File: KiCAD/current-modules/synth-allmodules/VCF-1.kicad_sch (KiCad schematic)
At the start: 0 parts

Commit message: VCF-1 Components Placed
Additions:
- Basic components for VCF-1
Changes:
- None
Removals:
- None
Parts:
- added C50: C, symbol Device:C
- added C51: C_Polarized, symbol Device:C_Polarized
- added Q12: 2N3906, Package_TO_SOT_THT:TO-92_Inline, symbol Transistor_BJT:2N3906
- added R98: R, symbol Device:R
- added RV37: R_Potentiometer, symbol Device:R_Potentiometer
- added SW17: SW_SPST, symbol Switch:SW_SPST
- added U15: TL074, symbol Amplifier_Operational:TL074
- added U16, U17: CA3080, symbol Amplifier_Operational:CA3080
- added U18: TL072, symbol Amplifier_Operational:TL072

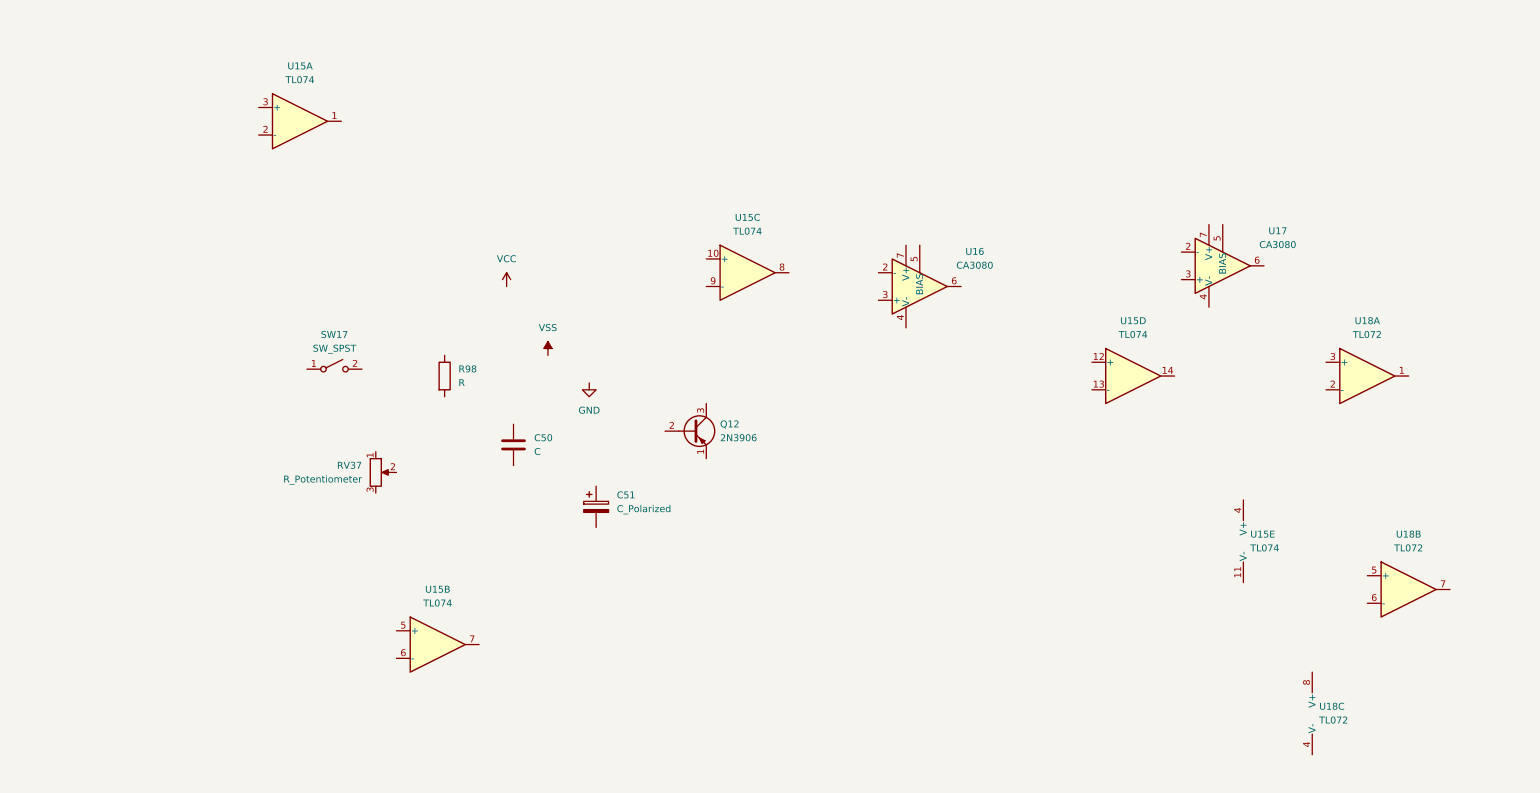
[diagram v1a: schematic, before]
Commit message: VCF-1 Component Placement
Additions:
- Most of the components for VCF-1 have been placed in the correct spots
Changes:
- None
Removals:
- None
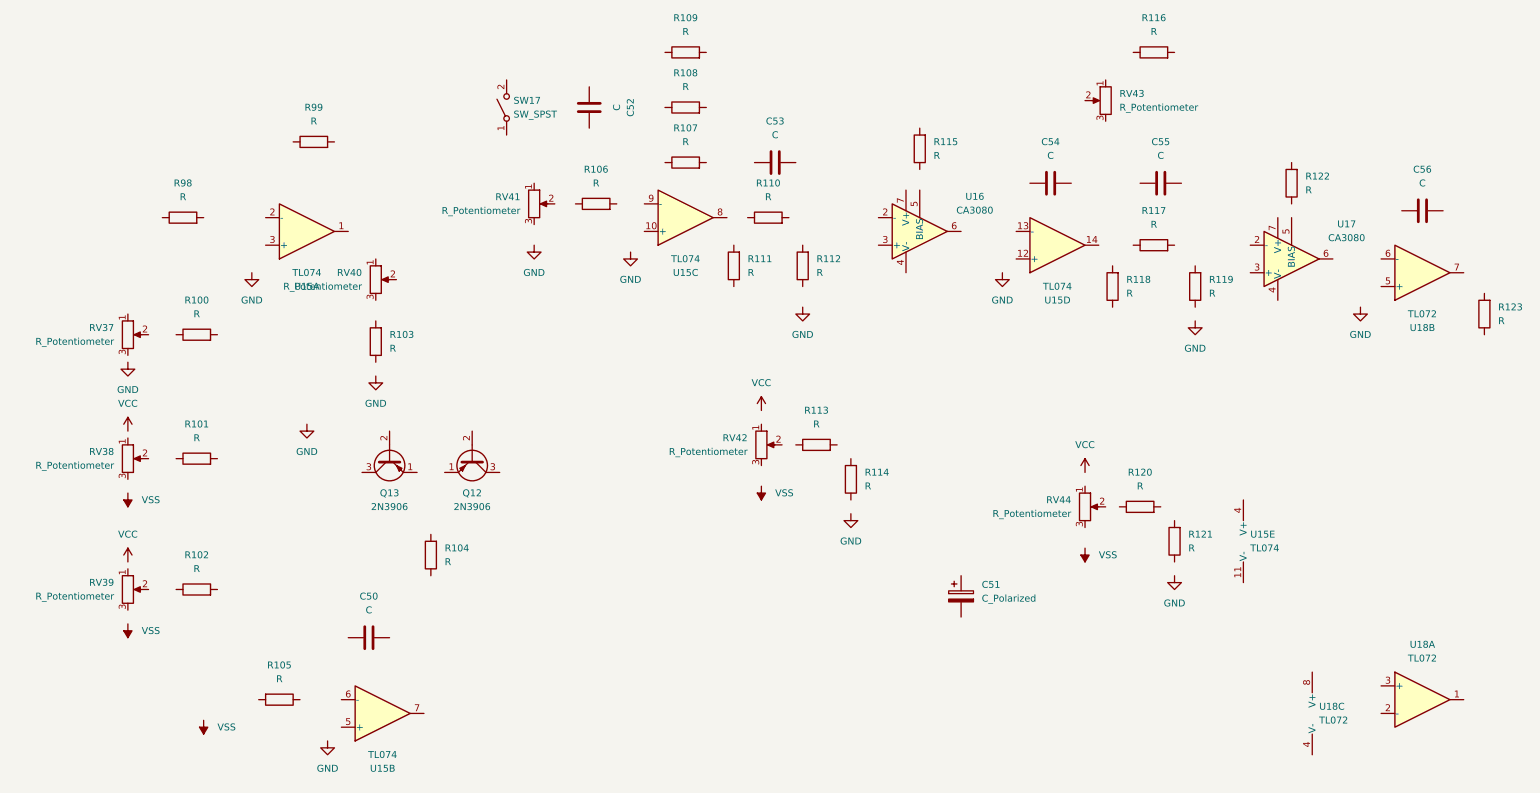
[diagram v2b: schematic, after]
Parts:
- added C52, C53, C54, C55, C56: C, symbol Device:C
- added Q13: 2N3906, Package_TO_SOT_THT:TO-92_Inline, symbol Transistor_BJT:2N3906
- added R100, R101, R102, R103, R104, R105, R106, R107, R108, R109, R110, R111, R112, R113, R114, R115, R116, R117, R118, R119, R120, R121, R122, R123, R99: R, symbol Device:R
- added RV38, RV39, RV40, RV41, RV42, RV43, RV44: R_Potentiometer, symbol Device:R_Potentiometer
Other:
- moved on the sheet: C50, C51, Q12, R98, RV37, SW17, U15A, U15B, U15C, U15D, U16, U17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

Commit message: Added Power Caps
Additions:
- Decoupling caps have been placed but need connection, along with the rest of the circuit
Changes:
- None
Removals:
- None
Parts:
- added C57, C58: C_Polarized, symbol Device:C_Polarized
- added C59, C60, C61, C62, C63, C64, C65, C66: C, symbol Device:C

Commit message: Started VCF-1 Connections
Additions:
- Connected some components on VCF
Changes:
- None
Removals:
- None
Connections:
- net GND: now also R103.1, R112.1, R114.1, R119.1, R121.1, RV37.3, RV41.3, U15.10 (+), U15.12 (+), U15.3 (+), U15.5 (+), U18.5 (+)
- net VCC: now also RV38.1, RV39.1, RV42.1, RV44.1
- net VSS: now also R105.2, RV38.3, RV39.3, RV42.3, RV44.3
- net at RV44.2: now also R120.1
- net at RV42.2: now also R113.1
- net at U18.6 (-): now also U17.6
- net at U15.14: now also R117.1, R118.2
- net at RV37.2: now also R100.1
- net at C50.1: now also R105.1, U15.6 (-)
- net at R121.2: now also R120.2
- net at R110.1: now also U15.8
- net at U15.9 (-): now also R106.2
- net at R119.2: now also R117.2, U17.2 (-)
- net at R98.2: now also U15.2 (-)
- net at R101.1: now also RV38.2
- net at R106.1: now also RV41.2
- net at R115.1: now also U16.5 (BIAS)
- net at RV40.3: now also R103.2
- net at U17.5 (BIAS): now also R122.1
- net at R102.1: now also RV39.2
